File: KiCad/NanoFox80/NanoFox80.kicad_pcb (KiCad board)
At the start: 2 copper layers, 90 x 37 mm, 84 parts, among them J101 Conn_01x02, J103 Conn_01x01, J104 Conn_01x02, J105 Conn_01x02, J106 Conn_01x02, J107 Conn_01x02, J108 Conn_01x01, J109 Conn_01x02, J110 I2C, J111 DB9 Female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

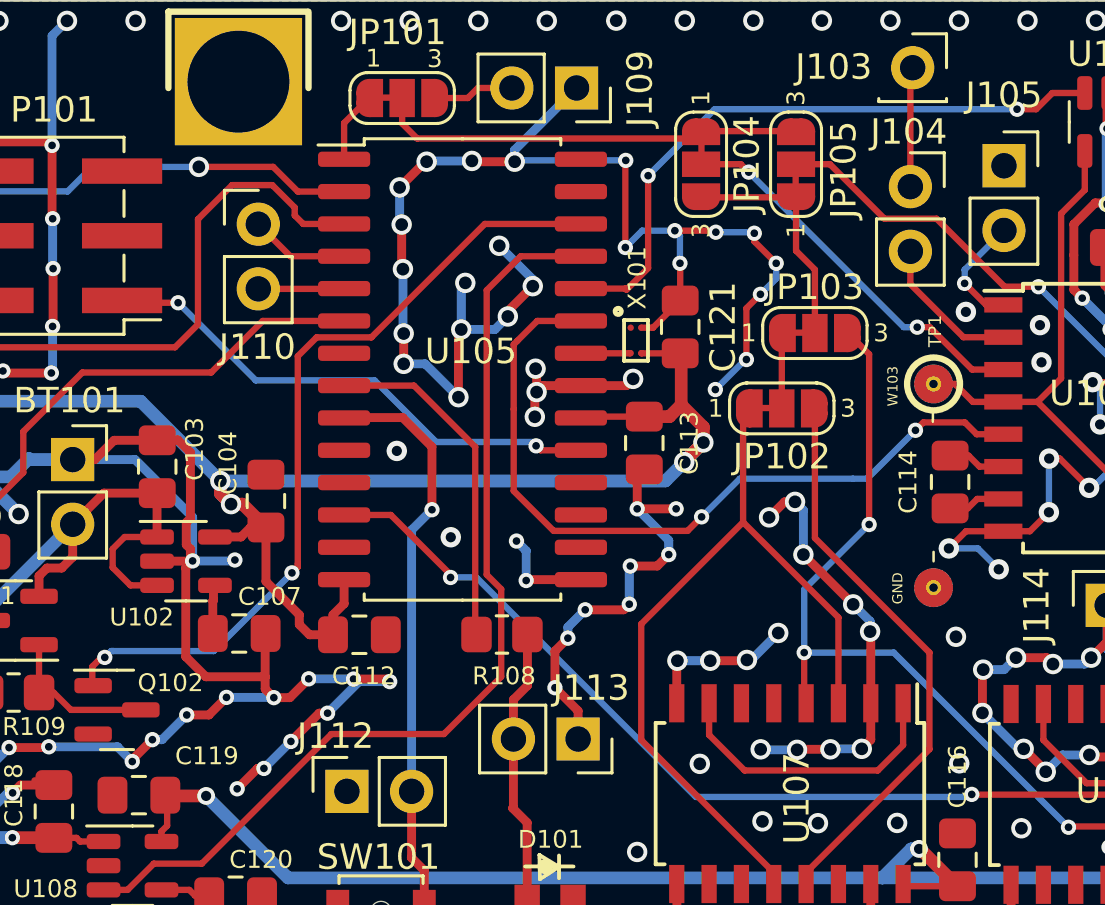
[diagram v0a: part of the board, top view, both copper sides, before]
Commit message: Schematic & PCB updates
o Moved X101 connection to U105
o Added header to pin 22 of U105
o Updated schematic and PCB
o Generated new Gerbers
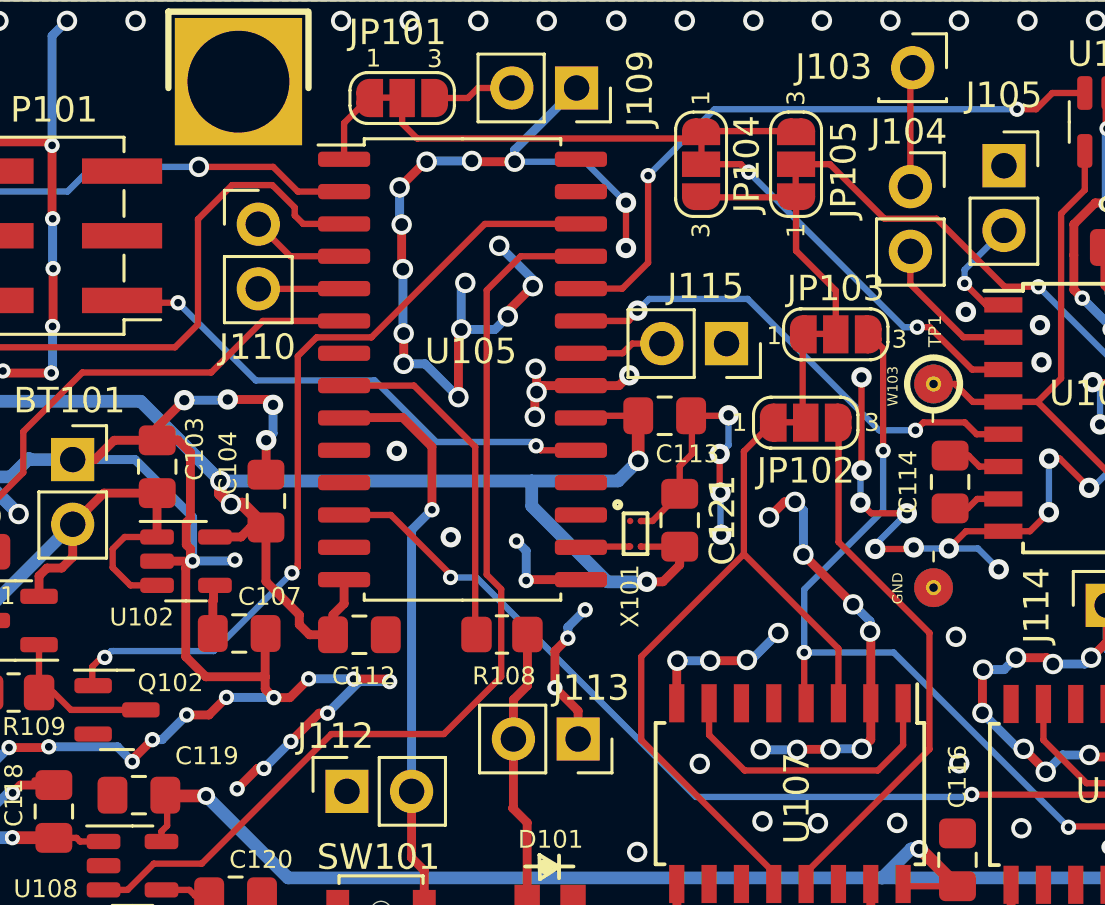
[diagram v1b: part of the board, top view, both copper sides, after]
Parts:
- added J115: Conn_01x02, Connector_PinSocket_2.54mm:PinSocket_1x02_P2.54mm_Vertical, F.Cu at (121.2, 69.5)
- moved C121 7.59 mm to (119.3, 76.4)
- moved X101 7.59 mm to (117.6, 76.9)
- moved C113 1.34 mm to (118.8, 72.3), turned to 180 degrees
- moved JP102 1.09 mm to (124.3, 72.6)
- moved JP103 0.82 mm to (125.5, 69.1)
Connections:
- U105 pad 16: unconnected-(U105-Pad16) -> Net-(U105-Pad16)
- X101 pad 2: Net-(U105-Pad22) -> Net-(U105-Pad16)
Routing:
- net Net-(U104-Pad5): track 30.6 -> 19.4 mm
- net GND: track 359.0 -> 361.6 mm, vias 228 -> 229
- net Net-(U105-Pad16): track 0.00 -> 1.93 mm
- net Net-(JP102-Pad1): track 31.2 -> 29.8 mm
- net Net-(U105-Pad22): track 1.93 -> 3.34 mm
- net +3V3: track 67.4 -> 68.5 mm
- net Net-(JP102-Pad3): track 22.6 -> 21.6 mm
- net Net-(JP102-Pad2): track 2.96 -> 3.52 mm
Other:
- board text added: "NanoFox80 Rev: 2-May-2022"
- board text removed: "NanoFox80 Rev: 30-Apr-2022"

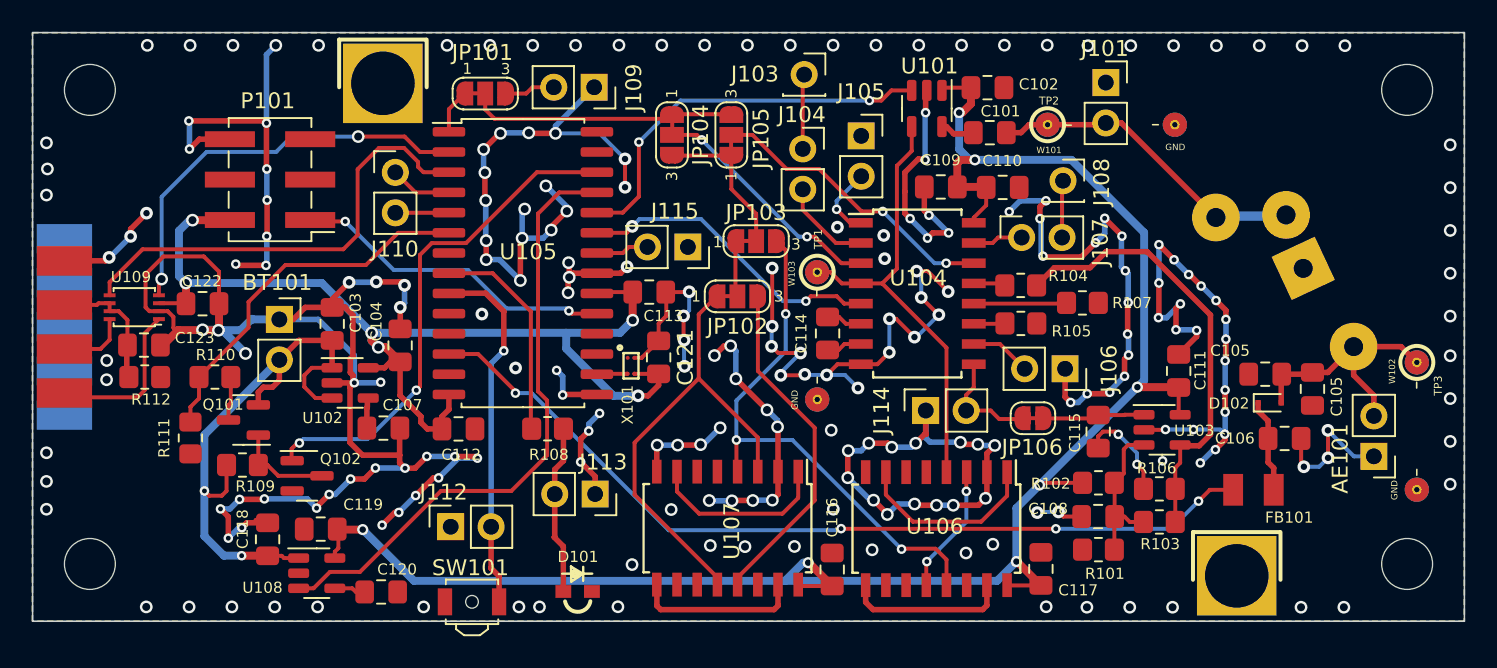
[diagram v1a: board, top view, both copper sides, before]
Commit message: Updated Footprints
o Corrected U106, U107 and U103 footprints
o Updated Gerbers
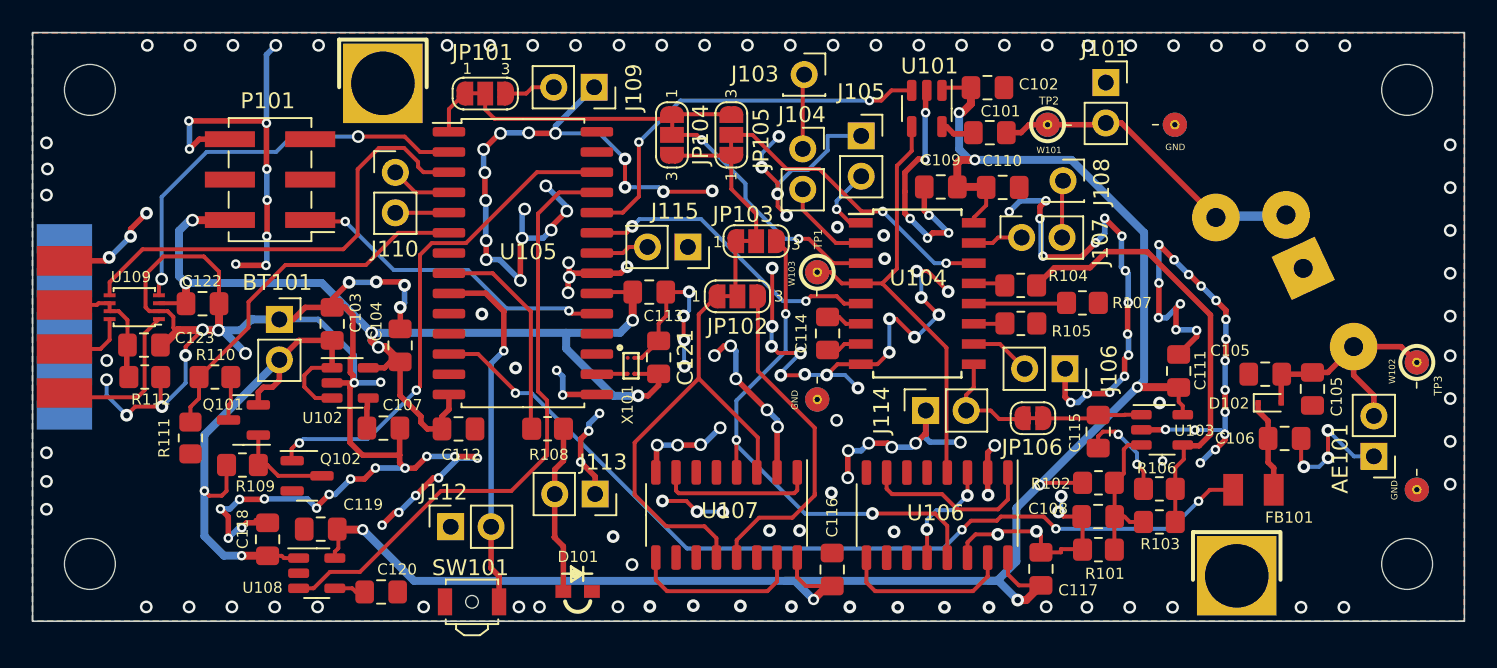
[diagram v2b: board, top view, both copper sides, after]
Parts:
- U106, U107: footprint Package_SO:SOIC-16W_5.3x10.2mm_P1.27mm -> Package_SO:SOIC-16_3.9x9.9mm_A_P1.27mm
- moved U106 0.85 mm to (136.9, 86.3)
- moved U107 0.83 mm to (123.6, 86.3)
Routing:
- net GND: track 361.6 -> 391.5 mm, vias 229 -> 239
- net +5V: track 115.2 -> 119.8 mm
- net Net-(FB101-Pad2): track 55.0 -> 56.6 mm
- net Net-(U107-Pad1): track 11.5 -> 10.0 mm
- net Net-(U106-Pad12): track 8.15 -> 7.01 mm
- net Net-(U106-Pad1): track 11.9 -> 11.1 mm
- net Net-(U106-Pad15): track 10.3 -> 11.0 mm
- net Net-(U107-Pad15): track 10.5 -> 11.1 mm
- net Net-(JP104-Pad2): track 15.2 -> 15.8 mm

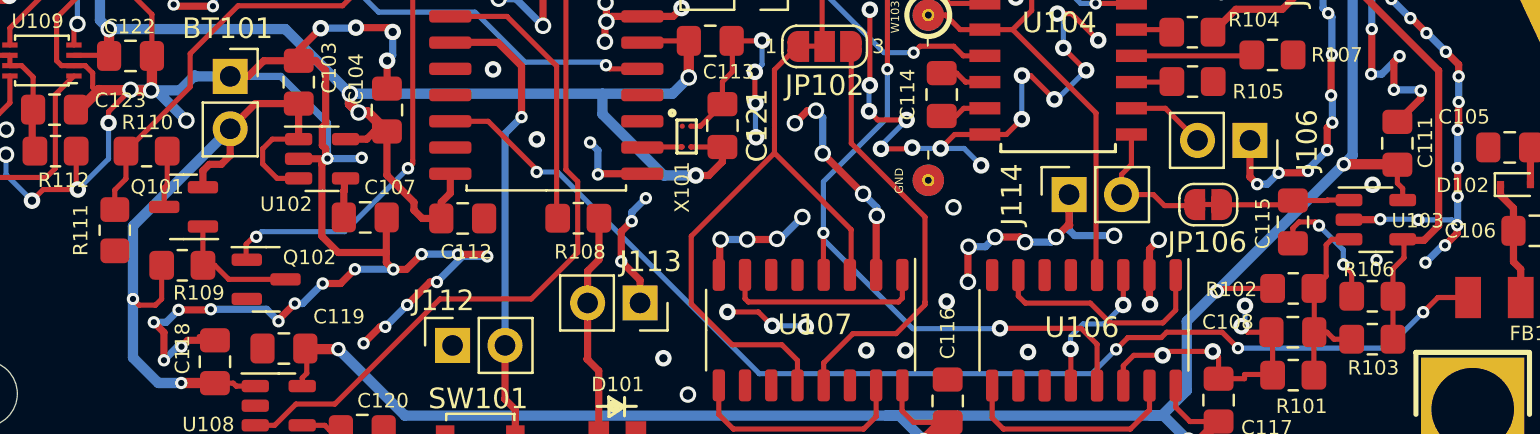
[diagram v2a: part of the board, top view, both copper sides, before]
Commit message: Schematic & PCB Updates
o Fixed pinout of Q101
o Changed device for U103
o Corrected PCB for Q101 change
o Updated PCB Rev
o Updated BOM
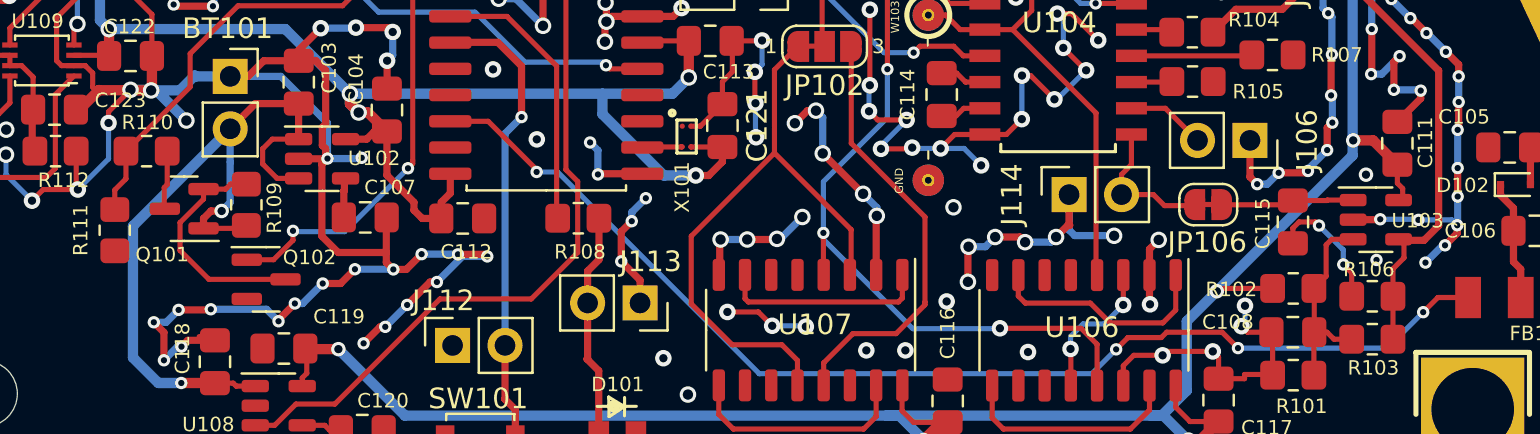
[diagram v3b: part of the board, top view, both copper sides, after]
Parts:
- Q101: value BSS84 -> BSS84T116
- U103: value OPA197 -> LMV721M5
- moved R109 4.27 mm to (96.3, 80.2), turned to 90 degrees
- moved Q101 0.09 mm to (93.3, 80.4)
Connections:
- Q101 pad 1: Net-(Q101-Pad1) -> +BATT
- Q101 pad 2: +BATT -> Net-(Q102-Pad3)
- Q102 pad 3: Net-(Q101-Pad1) -> Net-(Q102-Pad3)
- R109 pad 2: Net-(Q101-Pad1) -> Net-(Q102-Pad3)
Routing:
- net Net-(Q102-Pad3): track 0.00 -> 11.3 mm
- net Net-(Q101-Pad1): track 6.16 -> 0.00 mm
- net +BATT: track 36.8 -> 37.6 mm
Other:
- board text added: "NanoFox80 Rev: 3-May-2022"
- board text removed: "NanoFox80 Rev: 2-May-2022"

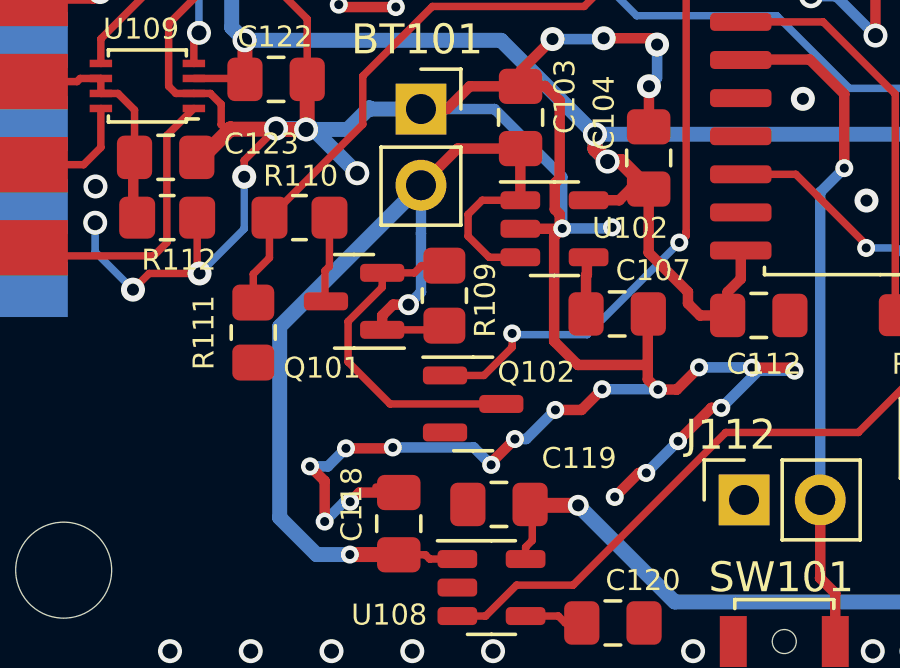
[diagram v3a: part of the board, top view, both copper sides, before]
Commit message: Schematic, BOM and PCB Updates
o Changed parts spec'd for Q101 and Q102
o Updated footprints
o Updated PCB
o Updated Gerbers
o Updated BOM
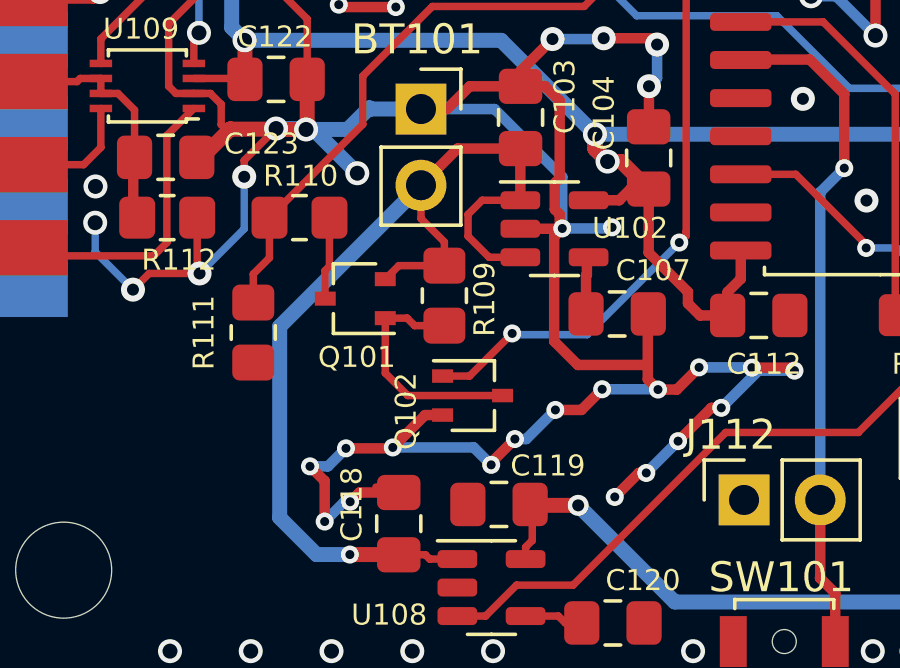
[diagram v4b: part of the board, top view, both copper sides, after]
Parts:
- Q101: value BSS84T116 -> BSS84W-7-F; footprint Package_TO_SOT_SMD:SOT-23 -> Package_TO_SOT_SMD:SOT-323_SC-70
- Q102: value BSS138 -> BSS138W-7-F; footprint Package_TO_SOT_SMD:SOT-23 -> Package_TO_SOT_SMD:SOT-323_SC-70
- moved Q102 0.28 mm to (97.2, 83.6)
- moved Q101 0.10 mm to (93.3, 80.3)
- turned R109 to -90 degrees
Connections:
- Q101 pad 1: +BATT -> Net-(Q102-Pad3)
- Q101 pad 2: Net-(Q102-Pad3) -> +BATT
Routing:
- net Net-(Q102-Pad3): track 11.3 -> 8.12 mm
- net +BATT: track 37.6 -> 34.9 mm, vias 2 -> 1
- net GND: track 391.5 -> 393.6 mm
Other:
- board text added: "NanoFox80 Rev: 4-May-2022"
- board text removed: "NanoFox80 Rev: 3-May-2022"

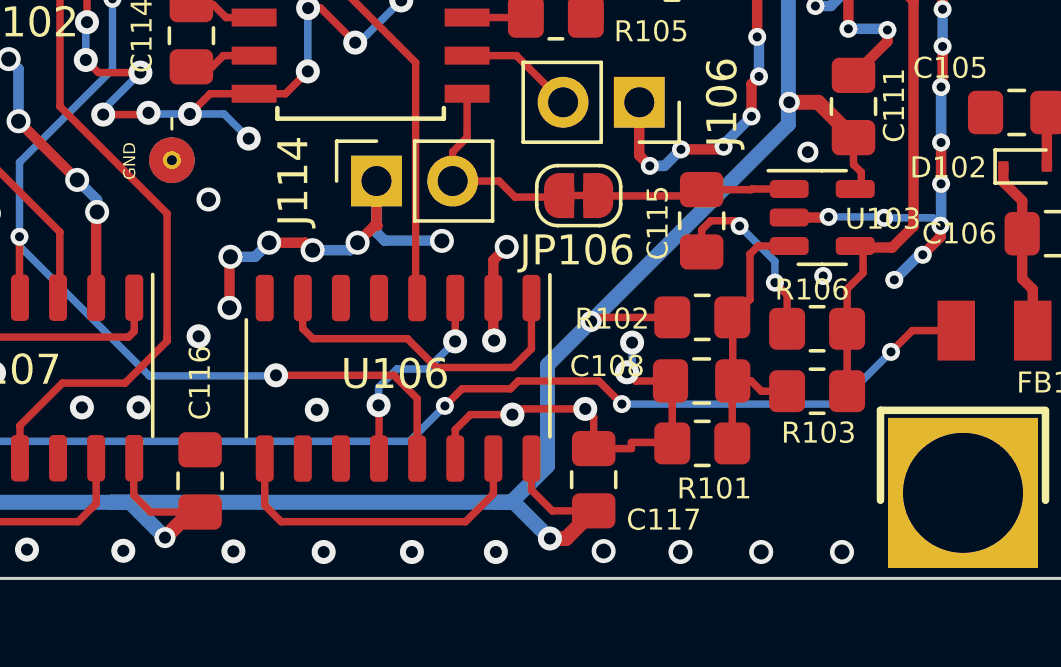
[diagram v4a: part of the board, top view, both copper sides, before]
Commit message: PCB Update
o Corrected footprint for U103
o Updated Gerbers
o Updated BOM
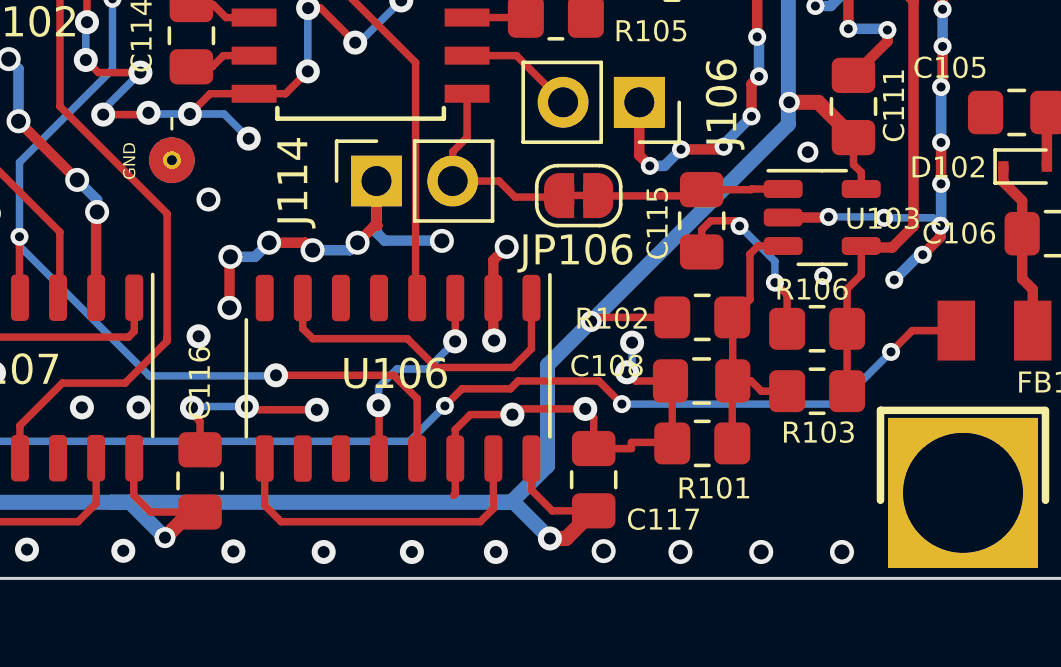
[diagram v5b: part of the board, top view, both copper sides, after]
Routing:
- net GND: track 393.6 -> 400.6 mm, vias 239 -> 241
